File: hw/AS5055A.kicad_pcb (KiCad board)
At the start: 2 copper layers, 54.7 x 42.3 mm, 30 parts, among them P1 CONN_8, P2 CONN_4, P3 CONN_4, P4 CONN_4, P5 CONN_2, SW1 Home, SW2 Calibrate, SW3 Passive, U1 ARDUINO_NANO, U2 TXB0108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

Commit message: Fixed some text consistency issues with the silk mask.
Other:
- board text added: "3V3"
- board text removed: "3v3"
- board text removed: "5v"
- board text removed: "Gnd"

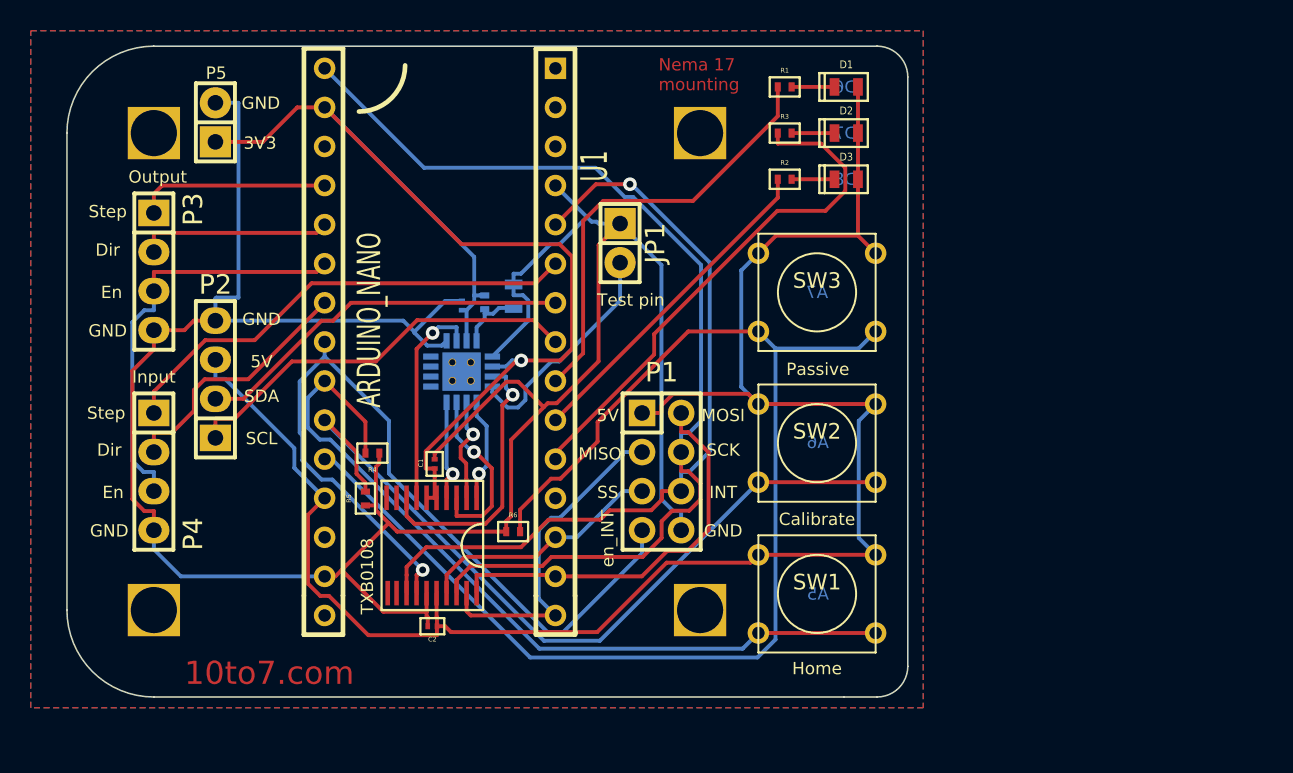
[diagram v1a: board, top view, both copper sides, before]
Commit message: Updated with revised arduino nano footprint
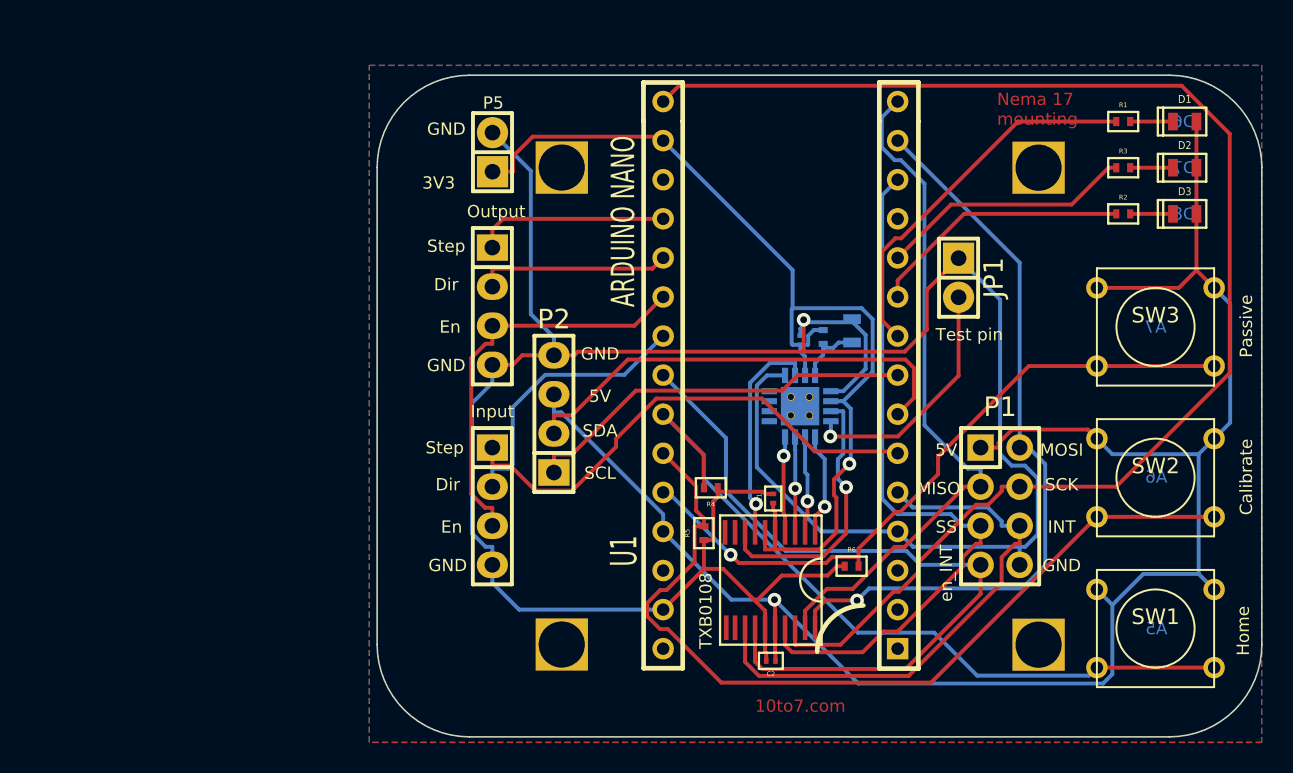
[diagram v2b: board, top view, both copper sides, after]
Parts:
- U1: value ARDUINO_NANO -> ARDUINO NANO
- moved 3mmHole_1 26.6 mm to (117.5, 82.7)
- moved 3mmHole_4 26.6 mm to (117.5, 113.7)
- moved C3 22.1 mm to (133.0, 94.0)
- moved JP1 22.1 mm to (143.3, 89.9)
- moved 3mmHole_2 22.1 mm to (148.5, 82.8)
- moved 3mmHole_3 22.1 mm to (148.5, 117.2)
- moved C1 22.1 mm to (131.2, 104.2)
- moved C2 22.1 mm to (131.1, 114.8)
- moved C4 22.1 mm to (136.4, 93.3)
- moved D1 22.1 mm to (158.0, 79.8)
- moved D2 22.1 mm to (158.0, 82.8)
- moved D3 22.1 mm to (158.0, 85.8)
- moved P1 22.1 mm to (146.0, 104.8)
- moved P2 22.1 mm to (117.0, 98.8)
- moved P3 22.1 mm to (113.0, 91.8)
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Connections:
- U1 pad 1: Net-(U1-Pad1) -> (no net)
- U1 pad 12: Net-(U1-Pad12) -> (no net)
- U1 pad 18: Net-(U1-Pad18) -> (no net)
- U1 pad 2: Net-(U1-Pad2) -> (no net)
- U1 pad 28: Net-(U1-Pad28) -> (no net)
- U1 pad 3: Net-(U1-Pad3) -> (no net)
- U1 pad 30: Net-(U1-Pad30) -> (no net)
- U2 pad 10: Net-(U2-Pad10) -> (no net)
- U2 pad 11: Net-(U2-Pad11) -> (no net)
- U2 pad 12: Net-(U2-Pad12) -> (no net)
- U2 pad 9: Net-(U2-Pad9) -> (no net)
- U3 pad 5: Net-(U3-Pad5) -> (no net)
- U3 pad 6: Net-(U3-Pad6) -> (no net)
- U3 pad 7: Net-(U3-Pad7) -> (no net)
- U3 pad 8: Net-(U3-Pad8) -> (no net)
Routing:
- net /Passive: track 85.0 -> 44.6 mm, vias 0 -> 1
- net /SS_B: track 16.1 -> 46.8 mm
- net /SCK_B: track 66.1 -> 91.3 mm
- net /MOSI_B: track 26.2 -> 49.4 mm, vias 0 -> 1
- net /MISO_B: track 22.0 -> 44.8 mm
- net /Status_3: track 34.3 -> 16.6 mm
- net /INT_B: track 51.1 -> 35.1 mm, vias 1 -> 0
- net +3.3V: track 73.1 -> 65.3 mm
- net /En_INT_B: track 54.6 -> 48.7 mm, vias 1 -> 0
- net /SCK_A: track 11.6 -> 6.21 mm
- net /Calibrate: track 51.8 -> 56.9 mm
- net /SDA: track 24.7 -> 29.7 mm
- net /Status_2: track 21.6 -> 17.1 mm
- net /Status_1: track 28.5 -> 24.6 mm
- net /Home: track 52.6 -> 49.8 mm
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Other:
- board size 54.7 x 42.3 mm -> 57.5 x 43 mm
- board text added: "AS5055A breakout board v0.2 Pin Mapping INT : D2 SS : D10 MOSI : D11 MISO : D12 SCK : D13 Enable Interupt : A2"
- board text removed: "AS5055A breakout board v0.1 Pin Mapping INT : D2 SS : D10 MOSI : D11 MISO : D12 SCK : D13 Enable Interupt : A2"
